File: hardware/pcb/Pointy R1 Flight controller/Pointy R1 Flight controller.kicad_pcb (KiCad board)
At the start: 2 copper layers, 58 x 100 mm, 30 parts, among them IC1 TEENSY_4.1, J3 XT60-M, M1 Motor_Servo, M2 Motor_Servo, P1 282837-2, P2 282837-2, P3 282837-2, P4 282837-2, Q1 IRLZ44NSTRLPBF, Q2 IRLZ44NSTRLPBF, Q3 IRLZ44NSTRLPBF, U1 L7805CV, U2 GY-521, U3 MPL3115A2

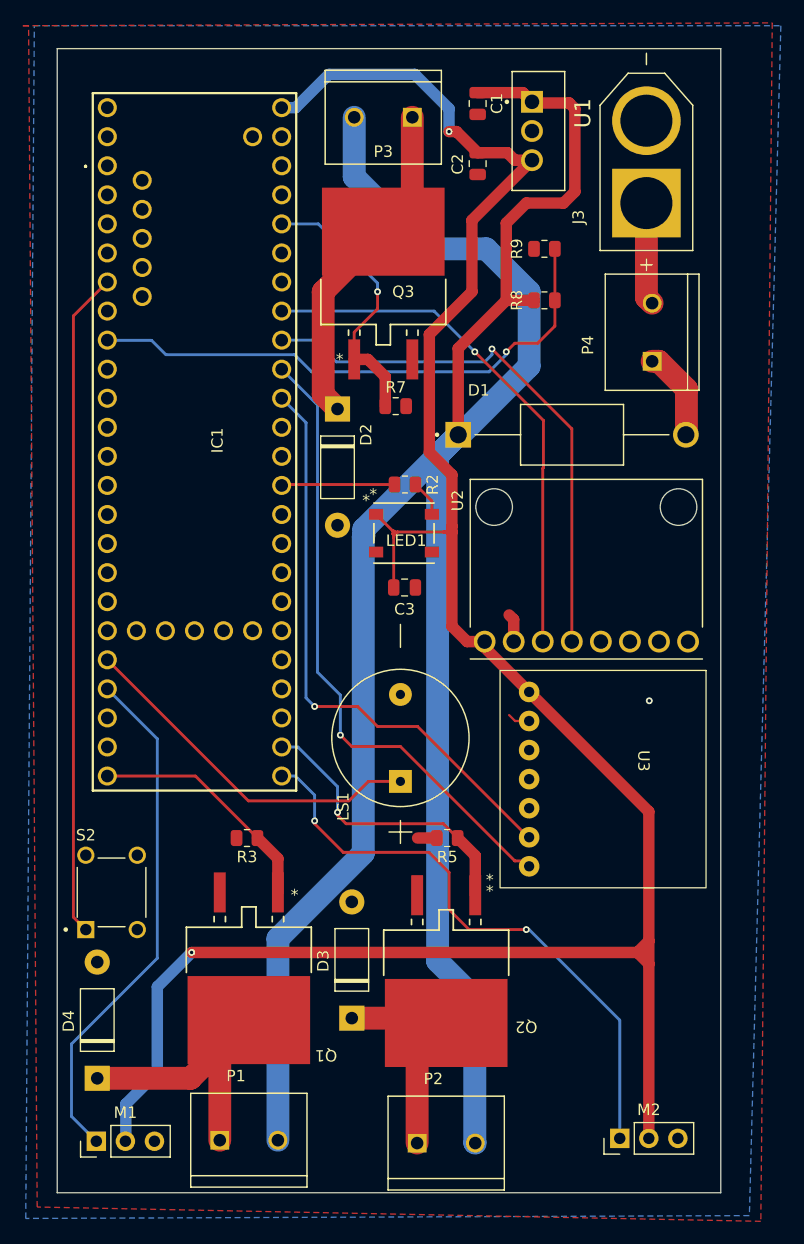
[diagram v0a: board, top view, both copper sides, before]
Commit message: Ran DFM + updated pcb accordingly. New gbr files generated
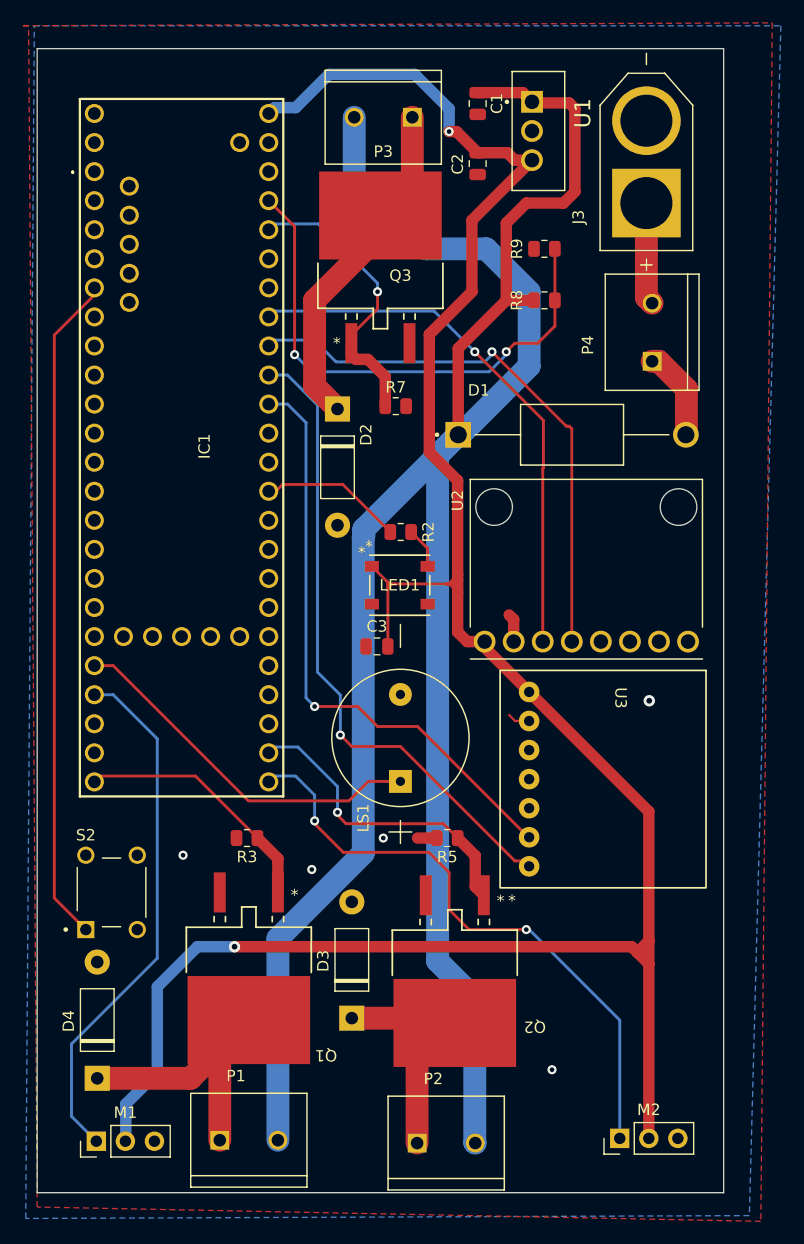
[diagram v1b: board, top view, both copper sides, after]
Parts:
- moved C3 5.69 mm to (143.9, 113.0), turned to 180 degrees
- moved LED1 4.57 mm to (145.9, 107.6)
- moved R2 4.17 mm to (146.0, 103.0)
- moved Q3 1.43 mm to (144.2, 78.5)
- moved IC1 1.24 mm to (119.2, 71.5)
- moved Q2 0.75 mm to (150.8, 142.8)
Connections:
- IC1 pad 23: unconnected-(IC1-A9-Pad23) -> VOL
- IC1 pad 7: VOL -> unconnected-(IC1-RX2-Pad7)
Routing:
- net +5V: track 200.7 -> 205.9 mm
- net LED: track 9.90 -> 12.6 mm
- net VOL: track 48.8 -> 46.3 mm, vias 1 -> 2
- net Net-(D2-A): track 29.2 -> 31.3 mm
- net PY2: track 25.8 -> 27.4 mm
- net PY3: track 23.9 -> 25.4 mm
- net TVC_Y: track 52.1 -> 53.4 mm
- net SCL: track 46.2 -> 47.5 mm
- net PY1: track 20.9 -> 22.2 mm
- net SDA: track 48.4 -> 49.4 mm
- net SDA1: track 55.4 -> 56.3 mm
- net SCL1: track 51.6 -> 52.5 mm
- net TVC_X: track 45.4 -> 46.3 mm
- net BUZ: track 31.4 -> 32.4 mm
- net Net-(D3-A): track 20.0 -> 20.7 mm
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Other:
- board size 58 x 100 mm -> 60 x 100 mm
